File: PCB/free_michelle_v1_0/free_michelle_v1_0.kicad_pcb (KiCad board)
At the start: 2 copper layers, 100 parts, among them J1 Zworka_TX, J10 ARK, J11 ARK, J12 Zworka_Buzzer, J13 ARK, J14 ARK, J15 Gniazdo 5VP DC 5,5x2,5, J16 Gniazdo 9V DC 5,5x2,5, J2 Zworka_RX, J3 GROVE_SW, J4 ARK, J5 ARK, J6 ARK, J7 ARK, J8 GROVE_SW, J9 A02YYUW_GroveCON, K1 FINDER-36.11, K2 FINDER-36.11, K3 FINDER-36.11, K4 FINDER-36.11, K5 FINDER-36.11, K6 FINDER-36.11, K7 FINDER-36.11, K8 FINDER-36.11, Q1 MMBT4403_PNP, Q2 MMBT4403_PNP, Q3 MMBT4403_PNP, Q4 MMBT4403_PNP, Q5 BSS138, Q6 MMBT4403_PNP, Q7 MMBT4403_PNP, Q8 MMBT4403_PNP, Q9 MMBT4403_PNP, SW1 Rotary_Encoder, SW2 SW_Push, SW3 SW_Push, U1 EEPROM_24AA01, U2 ESP8266_NodeMCU_v2, U3 DS3231M_RTC, U4 NRF24L01_Breakout, U5 BMP280, U6 LD1117V33, U7 L7805, U8 LD1117V33

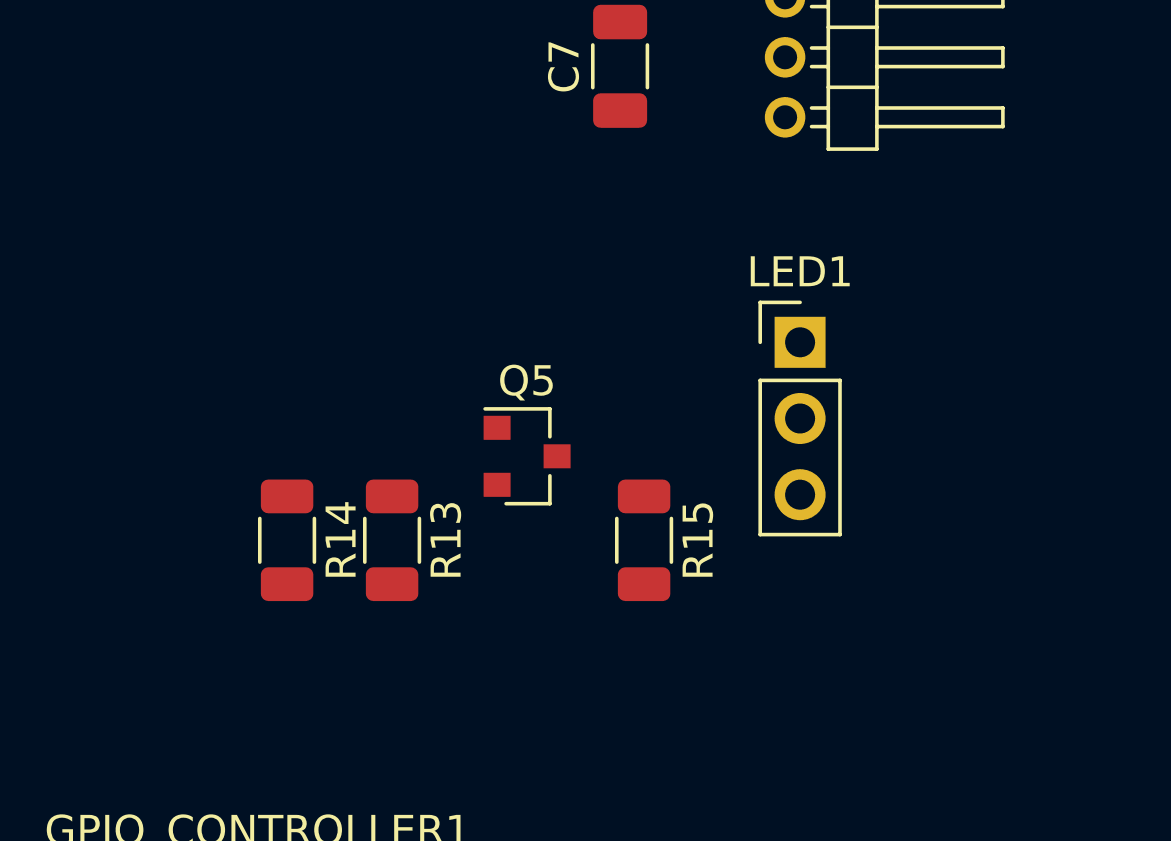
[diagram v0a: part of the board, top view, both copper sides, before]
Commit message: Zmienione zlacze dla WS2812b i dodany rezystor filtrujący napięcie
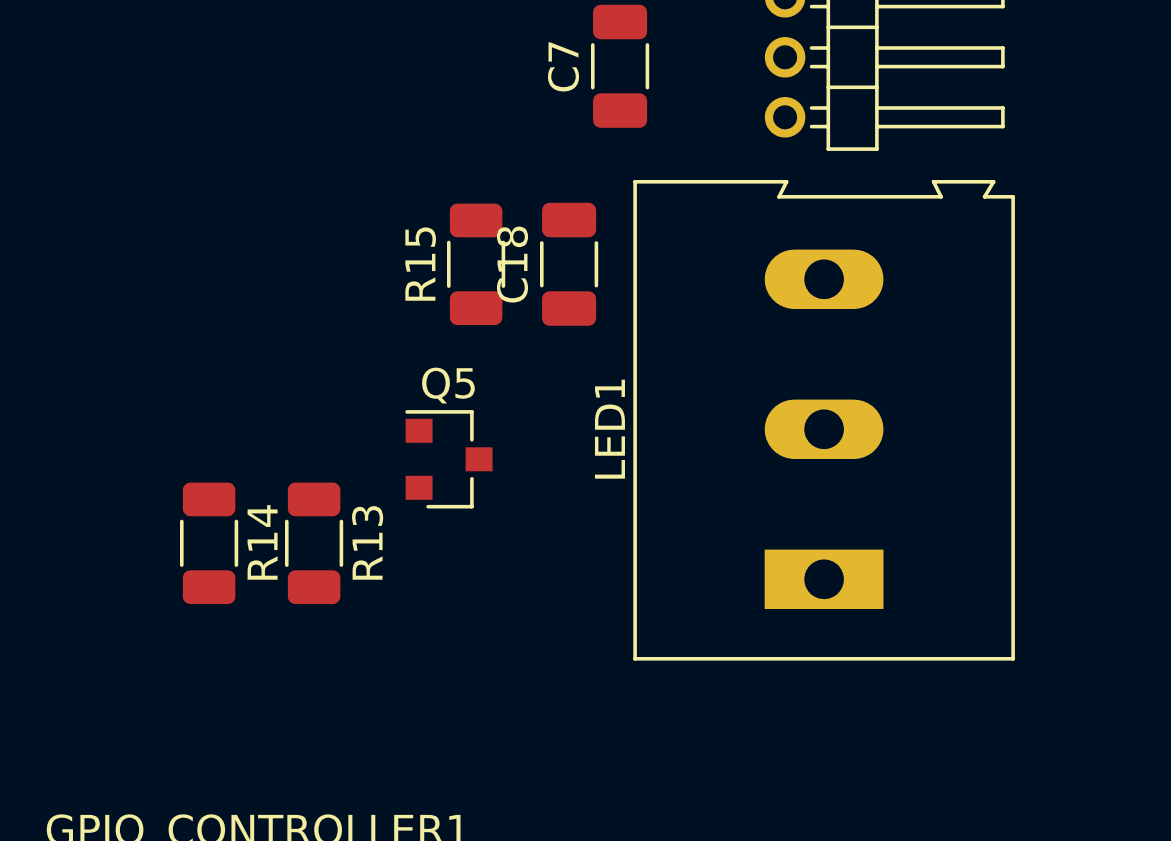
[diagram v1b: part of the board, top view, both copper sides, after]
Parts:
- added C18: 100nF, Capacitor_SMD:C_1206_3216Metric, F.Cu at (212.0, 79.8)
- LED1: footprint Connector_PinHeader_2.54mm:PinHeader_1x03_P2.54mm_Vertical -> TerminalBlock:TerminalBlock_Altech_AK300-3_P5.00mm
- moved R15 10.8 mm to (208.9, 79.8), turned to 90 degrees
- moved LED1 7.94 mm to (220.5, 90.3), turned to 90 degrees
- moved Q5 2.60 mm to (208.0, 86.3)
- moved R13 2.60 mm to (203.5, 89.1)
- moved R14 2.60 mm to (200.0, 89.1)

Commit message: Poprawki po rozmowie z Mackiem umieszczone na schemacie
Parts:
- removed C18: 100nF, Capacitor_SMD:C_1206_3216Metric
- added R22: 4K7, Resistor_SMD:R_1206_3216Metric, F.Cu at (195.5, 82.7)
- C7, C8: footprint Capacitor_SMD:C_1206_3216Metric -> Capacitor_THT:C_Disc_D5.0mm_W2.5mm_P2.50mm
- LED1: value WS2812b_ARK -> WS2812b_GROVE; footprint TerminalBlock:TerminalBlock_Altech_AK300-3_P5.00mm -> Connector_PinHeader_2.00mm:PinHeader_1x04_P2.00mm_Horizontal
- moved C8 175.8 mm to (39.1, 78.0), turned to 90 degrees
- moved C7 175.3 mm to (39.0, 87.8)
- moved J9 41.7 mm to (199.0, 90.9)
- moved LED1 34.0 mm to (199.0, 63.9), turned to 0 degrees
- moved SW2 30.3 mm to (32.8, 70.6)
- moved R12 28.2 mm to (50.5, 56.4), turned to 90 degrees
- moved R10 27.9 mm to (28.9, 56.6), turned to 90 degrees
- moved R9 27.8 mm to (131.0, 56.6), turned to 90 degrees
- moved R11 27.7 mm to (152.5, 56.6), turned to 90 degrees
- moved R16 27.5 mm to (174.5, 56.8), turned to 90 degrees
- moved R17 27.4 mm to (72.5, 56.4), turned to 90 degrees
- moved R18 27.4 mm to (196.6, 57.0), turned to 90 degrees
- moved R19 27.1 mm to (95.2, 56.4), turned to 90 degrees
- moved J15 25.6 mm to (31.6, 102.7)
- moved R14 24.7 mm to (189.2, 66.9), turned to 180 degrees
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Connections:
- C7 pad 1: +5V -> +5VP
- C8 pad 1: +5V -> +9V
- J3 pad 1: +3V3 -> Net-(J3-Pad1)
- J3 pad 2: Net-(J3-Pad2) -> GND
- J3 pad 4: GND -> +3V3
- J8 pad 1: +3V3 -> Net-(GPIO_CONTROLLER1-Pad42)
- J8 pad 2: Net-(GPIO_CONTROLLER1-Pad43) -> GND
- J8 pad 3: Net-(GPIO_CONTROLLER1-Pad42) -> Net-(GPIO_CONTROLLER1-Pad43)
- J8 pad 4: GND -> +3V3
- LED1 pad 1: +5VP -> Net-(LED1-Pad1)
- LED1 pad 2: Net-(LED1-Pad2) -> GND
- LED1 pad 3: GND -> Net-(LED1-Pad3)
- Q5 pad 3: Net-(LED1-Pad2) -> Net-(LED1-Pad3)
- R15 pad 1: Net-(LED1-Pad2) -> Net-(LED1-Pad3)
- TFT_CONTROLLER1 pad 42: Net-(J3-Pad3) -> Net-(J3-Pad1)
- TFT_CONTROLLER1 pad 43: Net-(J3-Pad2) -> Net-(J3-Pad3)
- Term1 pad 4: +5V -> +3V3

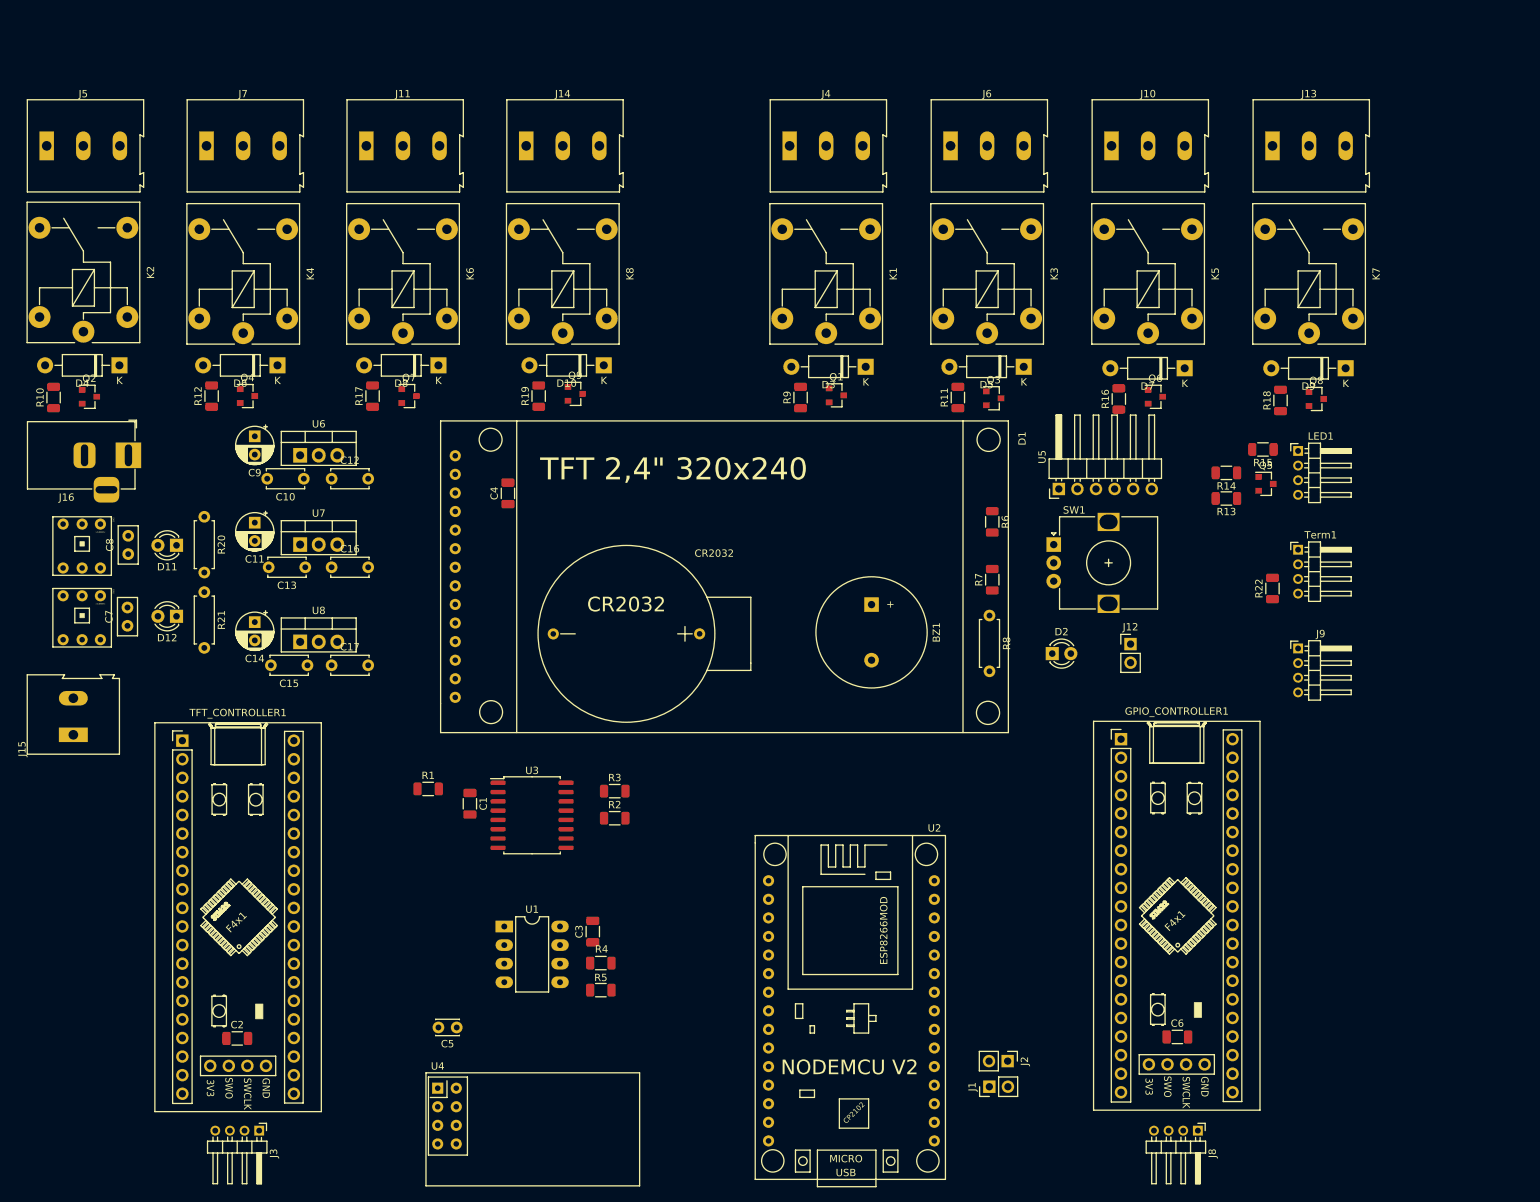
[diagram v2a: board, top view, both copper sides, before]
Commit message: Wykonane polaczenia dla TFT uC i zasilanie
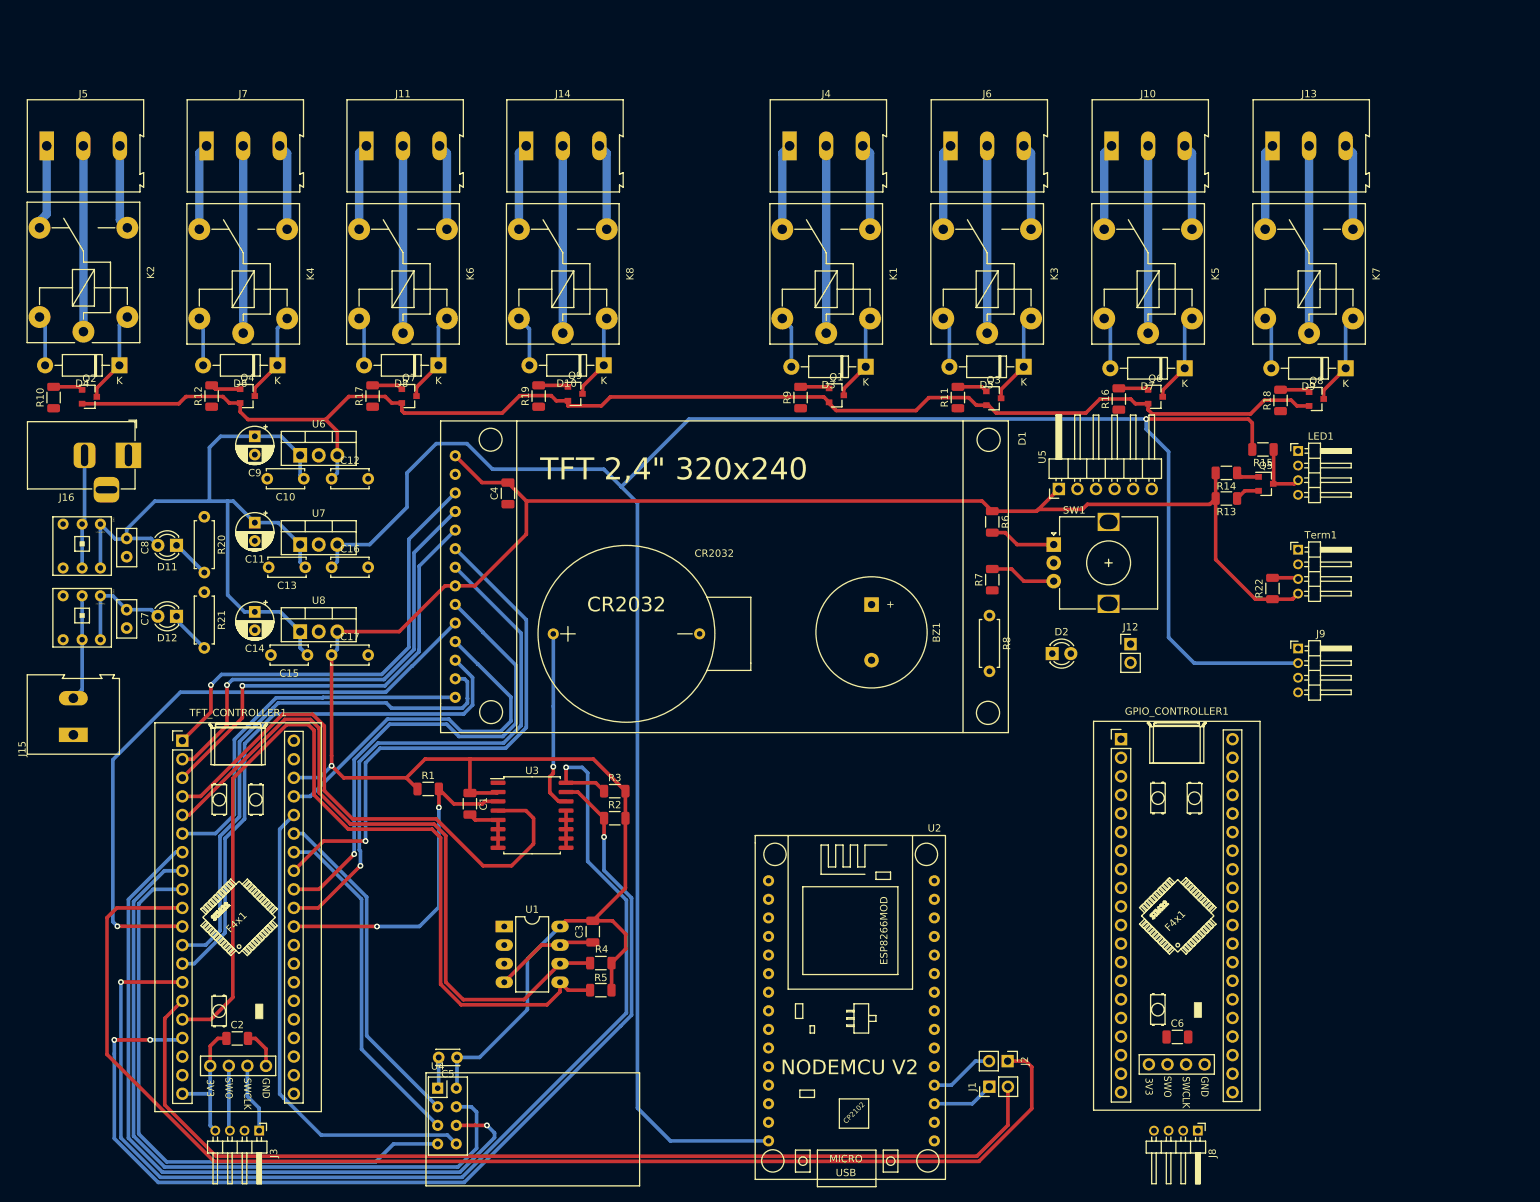
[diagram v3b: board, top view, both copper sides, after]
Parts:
- moved C5 4.10 mm to (84.0, 146.8)
- moved C7 2.20 mm to (38.9, 85.6), turned to 270 degrees
- moved C8 2.15 mm to (38.9, 75.9), turned to 270 degrees
- moved C15 1.40 mm to (63.6, 91.8)
- moved C17 1.40 mm to (66.9, 91.8)
- moved U8 1.40 mm to (62.6, 88.6)
- moved C14 1.40 mm to (56.4, 85.9)
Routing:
- net +3V3: track 0.00 -> 338.9 mm, vias 0 -> 1
- net +5V: track 0.00 -> 302.9 mm, vias 0 -> 1
- net +3.3VP: track 0.00 -> 190.2 mm
- net ESP_RX_TX_STM__U1_PA15: track 0.00 -> 174.3 mm
- net DS3231_SCL_PB6: track 0.00 -> 156.4 mm, vias 0 -> 2
- net DS3231_SDA_PB9: track 0.00 -> 141.0 mm, vias 0 -> 3
- net ESP_TX_RX_STM__U1_PB7: track 0.00 -> 140.4 mm
- net EEPROM_SDA_PB8: track 0.00 -> 125.2 mm
- net nRF24_MOSI_PA10: track 0.00 -> 102.9 mm, vias 0 -> 1
- net +9V: track 0.00 -> 100.8 mm
- net nRF24_CSN_PA11: track 0.00 -> 98.2 mm
- net EEPROM_SCL_PA8: track 0.00 -> 96.0 mm
- net GND: track 0.00 -> 92.6 mm
- net T_TFT_SCK_PB3: track 0.00 -> 86.5 mm, vias 0 -> 1
- net nRF24_MISO_PA12: track 0.00 -> 81.7 mm
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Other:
- net class 230V added: clearance 0.4, trace_width 1.15, via_dia 0.8, via_drill 0.4
- net class Default: trace_width 0.25 -> 0.5
